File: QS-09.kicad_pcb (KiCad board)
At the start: 2 copper layers, 57.2 x 61.9 mm, 49 parts, among them J1 TYPE-C-31-M12_13, SW1 Rotary_Encoder_Switch_Chassis, SW10 MXSwitch, SW11 MXSwitch, SW12 SW_Push, SW2 MXSwitch, SW3 MXSwitch, SW4 MXSwitch, SW5 Rotary_Encoder_Switch_Chassis, SW6 MXSwitch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

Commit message: USB ready, fixed RGB
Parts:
- moved C5 14.0 mm to (114.5, 46.2), turned to -135 degrees
- moved C4 13.6 mm to (109.3, 45.7), turned to -135 degrees
- moved Y1 10.1 mm to (111.4, 47.8), turned to -45 degrees
- moved C1 9.66 mm to (103.5, 51.9)
- moved C2 7.14 mm to (113.5, 51.4), turned to -45 degrees
- moved C3 6.34 mm to (107.1, 48.2), turned to 45 degrees
- moved U1 1.19 mm to (108.8, 55.2), turned to -135 degrees
- moved R4 0.08 mm to (110.5, 18.6)
- moved R5 0.08 mm to (126.0, 18.6)
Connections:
- C4 pad 2: Net-(C4-Pad2) -> GND
- C5 pad 1: Net-(C4-Pad2) -> GND
- D10 pad 2: Net-(D10-Pad2) -> UNDERGLOW
- D10 pad 4: RGB -> Net-(D10-Pad4)
- D11 pad 4: Net-(D10-Pad2) -> Net-(D12-Pad2)
- D12 pad 4: Net-(D11-Pad2) -> Net-(D15-Pad2)
- D13 pad 2: Net-(D13-Pad2) -> Net-(D10-Pad4)
- D13 pad 4: Net-(D12-Pad2) -> Net-(D14-Pad2)
- D14 pad 4: Net-(D13-Pad2) -> Net-(D11-Pad2)
- D15 pad 4: Net-(D14-Pad2) -> Net-(D18-Pad2)
- D16 pad 4: Net-(D15-Pad2) -> RGB
- D18 pad 2: UNDERGLOW -> Net-(D18-Pad2)
- D19 pad 4: UNDERGLOW -> Net-(D22-Pad2)
- D20 pad 2: Net-(D20-Pad2) -> unconnected-(D20-Pad2)
- D21 pad 4: Net-(D20-Pad2) -> UNDERGLOW
- D22 pad 2: unconnected-(D22-Pad2) -> Net-(D22-Pad2)
- U1 pad 14: RGB -> unconnected-(U1-Pad14)
- U1 pad 25: unconnected-(U1-Pad25) -> RGB
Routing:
- net +5V: track 0.00 -> 46.7 mm, vias 0 -> 2
- net GND: track 0.00 -> 32.7 mm
- net Net-(F1-Pad1): track 0.00 -> 26.7 mm, vias 0 -> 2
- net UD+: track 0.00 -> 24.5 mm
- net UD-: track 0.00 -> 23.7 mm
- net Net-(R1-Pad2): track 0.00 -> 12.9 mm
- net Net-(R2-Pad1): track 0.00 -> 12.9 mm
- net Net-(J1-PadA5): track 0.00 -> 7.88 mm
- net XTAL1: track 0.00 -> 6.65 mm
- net XTAL2: track 0.00 -> 6.43 mm
- net Net-(J1-PadB5): track 0.00 -> 5.92 mm
- net Net-(C1-Pad1): track 0.00 -> 2.26 mm
- net D-: track 0.00 -> 1.62 mm
- net D+: track 0.00 -> 1.60 mm
- added copper zone on B.Cu, net GND
- added copper zone on F.Cu, net GND

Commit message: alpha
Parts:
- removed R3: 10k, Resistor_SMD:R_0603_1608Metric
- removed SW12: SW_Push, Button_Switch_SMD:SW_SPST_SKQG_WithStem
- added Ref**: Val**, quark-works:quark-logo-small-v3, B.Cu at (128.7, 57.7)
- SW1, SW5: value Rotary_Encoder_Switch_Chassis -> Encoder
- moved D9 2.63 mm to (129.1, 69.2)
- moved D3 2.03 mm to (129.3, 28.3)
- moved D4 1.35 mm to (91.9, 46.4)
- turned D10 to 0 degrees
- turned D11 to 0 degrees
- turned D12 to 0 degrees
- turned D14 to 0 degrees
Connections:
- SW1 pad A: unconnected-(SW1-PadA) -> ENCA1
- SW1 pad B: unconnected-(SW1-PadB) -> ENCB1
- SW1 pad C: unconnected-(SW1-PadC) -> GND
- SW5 pad A: unconnected-(SW5-PadA) -> ENCA2
- SW5 pad B: unconnected-(SW5-PadB) -> ENCB2
- SW5 pad C: unconnected-(SW5-PadC) -> GND
- U1 pad 10: unconnected-(U1-Pad10) -> ENCB2
- U1 pad 13: unconnected-(U1-Pad13) -> COL1
- U1 pad 19: unconnected-(U1-Pad19) -> COL2
- U1 pad 20: unconnected-(U1-Pad20) -> ROW2
- U1 pad 21: unconnected-(U1-Pad21) -> ENCA1
- U1 pad 22: unconnected-(U1-Pad22) -> ENCB1
- U1 pad 23: unconnected-(U1-Pad23) -> COL0
- U1 pad 7: unconnected-(U1-Pad7) -> ROW0
- U1 pad 8: unconnected-(U1-Pad8) -> ROW1
- U1 pad 9: unconnected-(U1-Pad9) -> ENCA2
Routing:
- net +5V: track 46.7 -> 222.5 mm, vias 2 -> 5
- net Net-(D19-Pad4): track 0.00 -> 83.4 mm, vias 0 -> 2
- net COL2: track 0.00 -> 83.2 mm, vias 0 -> 1
- net ROW0: track 0.00 -> 75.2 mm, vias 0 -> 4
- net ROW1: track 0.00 -> 60.6 mm, vias 0 -> 2
- net COL0: track 0.00 -> 58.7 mm
- net COL1: track 0.00 -> 52.5 mm
- net GND: track 32.7 -> 76.9 mm, vias 0 -> 24
- net ENCB1: track 0.00 -> 41.7 mm, vias 0 -> 1
- net ENCB2: track 0.00 -> 40.3 mm, vias 0 -> 1
- net ENCA1: track 0.00 -> 40.3 mm, vias 0 -> 1
- net ROW2: track 0.00 -> 38.0 mm, vias 0 -> 2
- net ENCA2: track 0.00 -> 35.7 mm, vias 0 -> 1
- net RGB: track 0.00 -> 25.5 mm
- net Net-(D12-Pad4): track 0.00 -> 23.8 mm
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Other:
- board text added: "QS-09 alpha"
- board text added: "debido a que mis comentarios en broma han sido censurados me veo en la necesidad de expresarlos de manera directa.. El único alto impacto de este set a mi parecer es que es diseñado por Zambumon, fuera de eso, no difiere casi en nada a GMK Pulse en su variación Mitolet, o a GMK Serenity que es más pastel. GMK Pulse está en stock, entonces no tendrían que esperar 4 siglos, y Serenity se espera que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"
- board text removed: "QS-09"

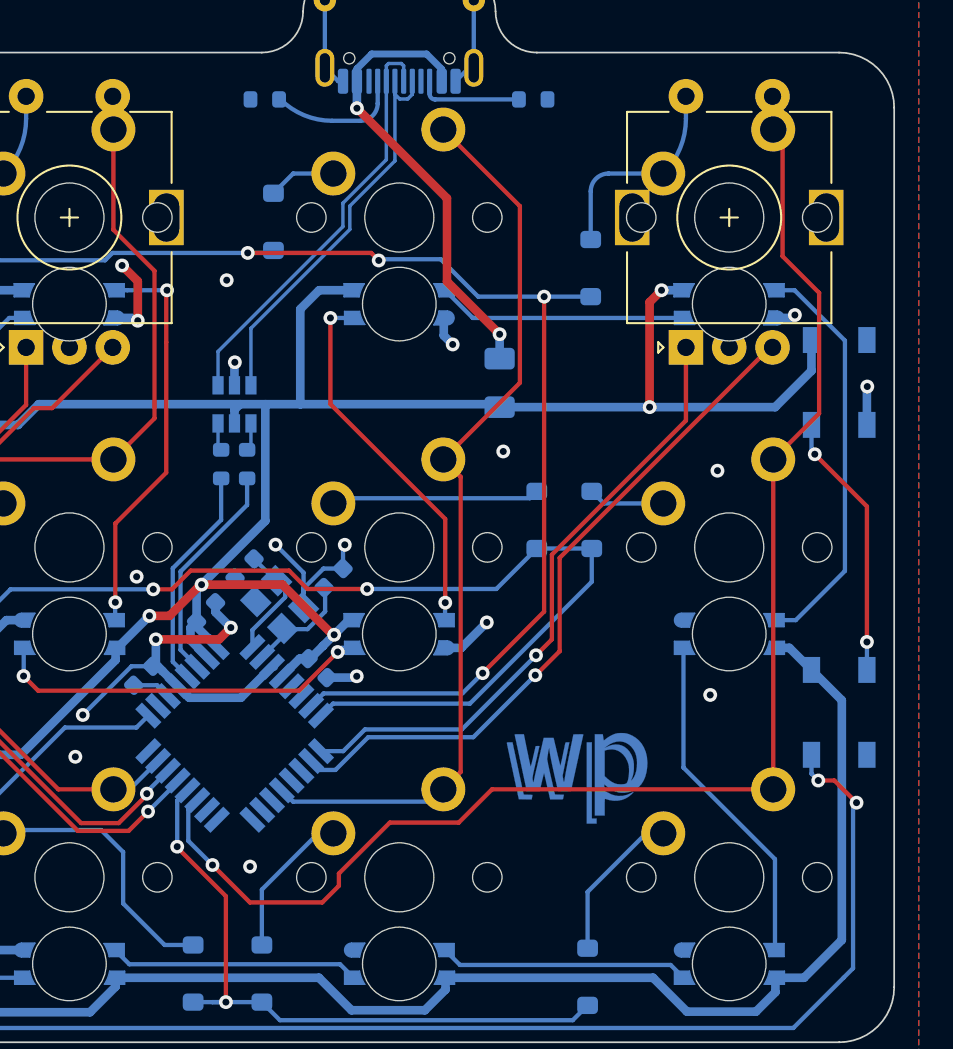
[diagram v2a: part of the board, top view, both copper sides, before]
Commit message: Added reset button, fixed a missing resistor
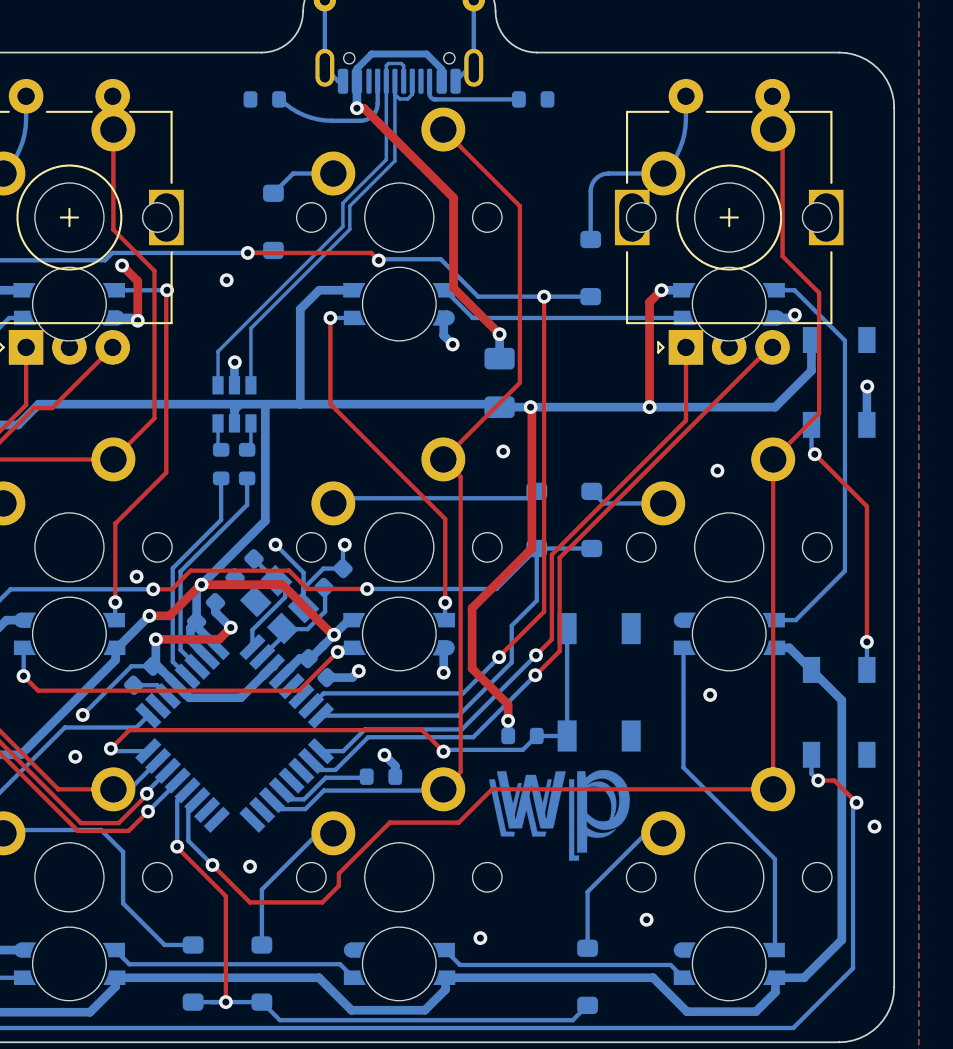
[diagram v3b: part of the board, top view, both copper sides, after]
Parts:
- added R3: 10k, Resistor_SMD:R_0603_1608Metric, B.Cu at (117.2, 57.7)
- added R6: 10k, Resistor_SMD:R_0603_1608Metric, B.Cu at (125.4, 55.3)
- added SW12: SW_Push, Button_Switch_SMD:SW_SPST_SKQG_WithStem, B.Cu at (129.8, 52.2)
- moved Ref** 2.37 mm to (127.7, 59.8)
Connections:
- U1 pad 13: COL1 -> Net-(U1-Pad13)
- U1 pad 14: unconnected-(U1-Pad14) -> COL1
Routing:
- net RESET: track 0.00 -> 36.1 mm, vias 0 -> 2
- net +5V: track 222.5 -> 243.9 mm, vias 5 -> 7
- net Net-(U1-Pad13): track 0.00 -> 5.66 mm
- net COL1: track 52.5 -> 54.2 mm
- net ROW1: track 60.6 -> 59.3 mm
- net GND: track 76.9 -> 77.0 mm, vias 24 -> 28
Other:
- board text added: "QS-09 alpha v0.2"
- board text removed: "QS-09 alpha"

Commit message: Fixed some wonky shit with the data lines
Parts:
- added Ref**: Val**, quark-works:iso, F.Cu at (118.3, 35.2)
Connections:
- J1 pad A6: UD- -> UD+
- J1 pad A7: UD+ -> UD-
- J1 pad B6: UD- -> UD+
- J1 pad B7: UD+ -> UD-
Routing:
- net COL2: track 83.2 -> 97.9 mm
- net Net-(D11-Pad2): track 21.5 -> 24.9 mm
- net ROW1: track 59.3 -> 57.5 mm
- net UD+: track 24.5 -> 25.4 mm, vias 0 -> 2
- net Net-(D9-Pad2): track 9.02 -> 9.92 mm
- net +5V: track 243.9 -> 243.3 mm
- net GND: vias 28 -> 27
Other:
- board text added: "QS-09 alpha v0.3"
- board text removed: "QS-09 alpha v0.2"

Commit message: New logo, version 1.0
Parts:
- removed the Ref** at (127.7, 59.8)
- added Ref**: Val**, qw new logo:qw-logo-small, B.Cu at (127.0, 60.3)
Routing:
- net COL2: track 97.9 -> 94.9 mm
- net GND: track 77.0 -> 75.2 mm
- net COL1: track 54.2 -> 53.1 mm
- net ENCB2: track 40.6 -> 40.0 mm
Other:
- board text added: "QS-09 v1.0"
- board text removed: "QS-09 alpha v0.3"
- board text removed: "debido a que mis comentarios en broma han sido censurados me veo en la necesidad de expresarlos de manera directa.. El único alto impacto de este set a mi parecer es que es diseñado por Zambumon, fuera de eso, no difiere casi en nada a GMK Pulse en su variación Mitolet, o a GMK Serenity que es más pastel. GMK Pulse está en stock, entonces no tendrían que esperar 4 siglos, y Serenity se espera que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"
